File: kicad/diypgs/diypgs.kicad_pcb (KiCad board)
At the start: 2 copper layers, 150 x 66 mm, 15 parts, among them SW1 SW_Push_Dual, SW2 SW_Push_Dual, SW3 SW_Push_Dual, SW4 SW_Push_Dual, SW5 SW_Push_Dual, SW6 SW_Push_Dual, U1 Nokia_5110_LCD

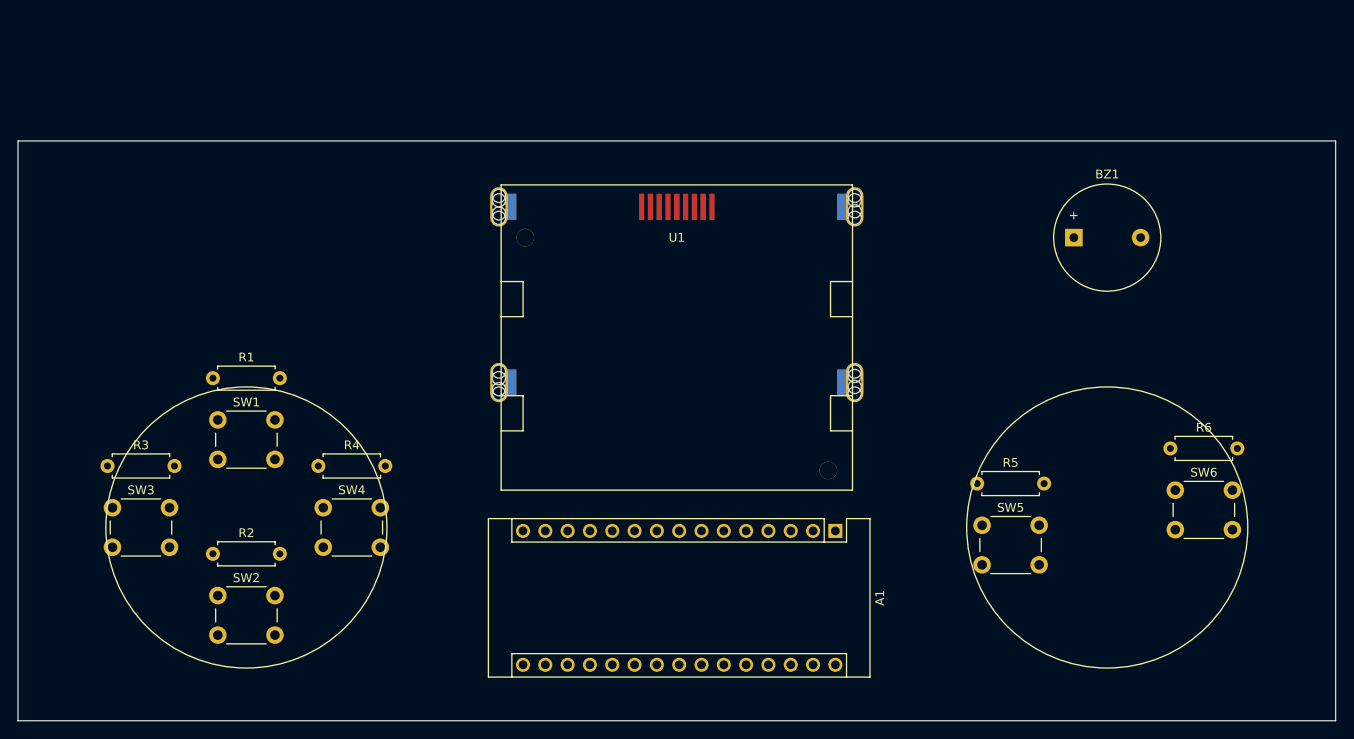
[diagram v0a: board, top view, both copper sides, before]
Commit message: Fix button pad number
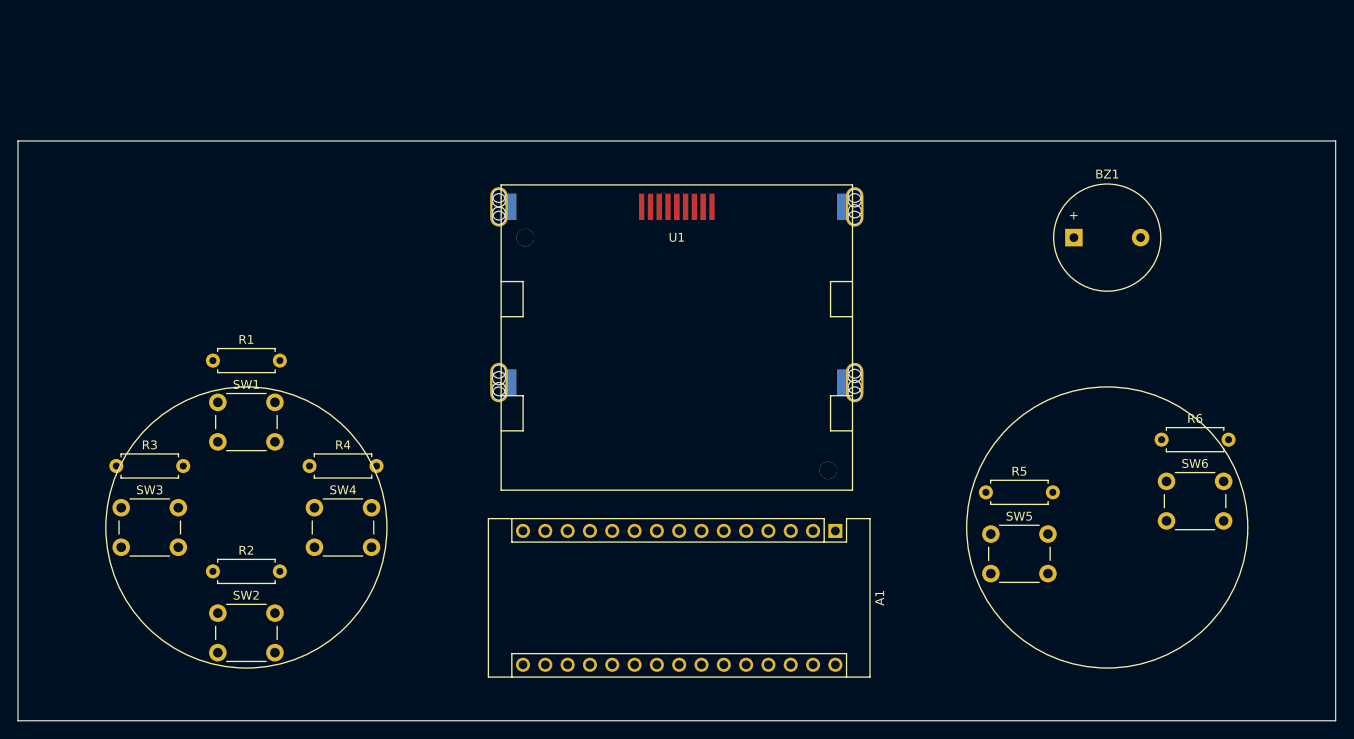
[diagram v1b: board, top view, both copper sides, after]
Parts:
- SW1, SW2, SW3, SW4, SW5, SW6: footprint Button_Switch_THT:SW_PUSH_6mm -> Footprints:SW_PUSH_6mm_ALT
- moved R1 2.00 mm to (72.2, 75.0)
- moved R2 2.00 mm to (72.2, 99.0)
- moved SW1 2.00 mm to (72.8, 79.8)
- moved SW2 2.00 mm to (72.8, 103.8)
- moved R5 1.41 mm to (160.2, 90.0)
- moved R6 1.41 mm to (180.2, 84.0)
- moved SW5 1.41 mm to (160.8, 94.8)
- moved SW6 1.41 mm to (180.8, 88.8)
- moved R3 1.00 mm to (61.2, 87.0)
- moved R4 1.00 mm to (83.2, 87.0)
- moved SW3 1.00 mm to (61.8, 91.8)
- moved SW4 1.00 mm to (83.8, 91.8)
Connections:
- R2 pad 1: Net-(R2-Pad1) -> Net-(SW2-Pad3)
- SW1 pad 1: Net-(R1-Pad1) -> +3V3
- SW1 pad 2: +3V3 -> unconnected-(SW1-Pad2)

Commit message: Add PCB tracks
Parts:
- moved SW5 7.91 mm to (167.2, 99.2), turned to 180 degrees
- moved SW6 7.91 mm to (187.2, 93.2), turned to 180 degrees
- moved R2 7.62 mm to (79.8, 99.0), turned to 180 degrees
- moved R5 7.62 mm to (167.8, 90.0), turned to 180 degrees
- moved R6 7.62 mm to (187.8, 84.0), turned to 180 degrees
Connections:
- A1 pad 10: /ARDUINO_PAD_B_PIN -> /ARDUINO_PAD_RIGHT_PIN
- A1 pad 11: /ARDUINO_BUZZER_PIN -> /ARDUINO_PAD_LEFT_PIN
- A1 pad 12: /ARDUINO_DC_PIN -> /ARDUINO_PAD_DOWN_PIN
- A1 pad 13: /ARDUINO_RESET_PIN -> /ARDUINO_PAD_UP_PIN
- A1 pad 5: /ARDUINO_PAD_UP_PIN -> /ARDUINO_PAD_B_PIN
- A1 pad 6: /ARDUINO_PAD_DOWN_PIN -> /ARDUINO_PAD_A_PIN
- A1 pad 7: /ARDUINO_PAD_LEFT_PIN -> /ARDUINO_BUZZER_PIN
- A1 pad 8: /ARDUINO_PAD_RIGHT_PIN -> /ARDUINO_RESET_PIN
- A1 pad 9: /ARDUINO_PAD_A_PIN -> /ARDUINO_DC_PIN
- SW5 pad 4: /ARDUINO_PAD_A_PIN -> /ARDUINO_PAD_B_PIN
- SW6 pad 4: /ARDUINO_PAD_B_PIN -> /ARDUINO_PAD_A_PIN
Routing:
- net +3V3: track 0.00 -> 133.5 mm
- net GND: track 0.00 -> 110.8 mm
- net /ARDUINO_BUZZER_PIN: track 0.00 -> 64.9 mm
- net /ARDUINO_PAD_A_PIN: track 0.00 -> 53.4 mm
- net /ARDUINO_PAD_B_PIN: track 0.00 -> 29.3 mm
- net Net-(R6-Pad1): track 0.00 -> 4.98 mm
- net Net-(R5-Pad1): track 0.00 -> 4.98 mm

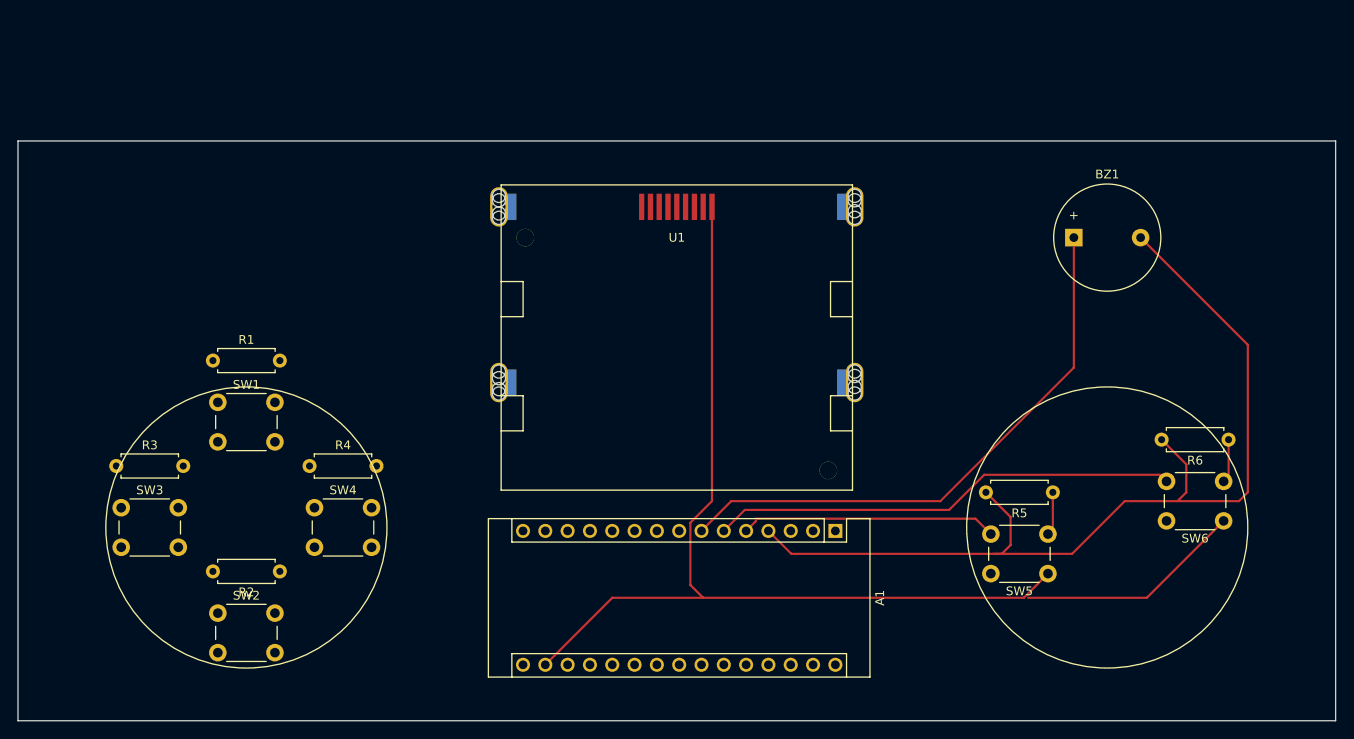
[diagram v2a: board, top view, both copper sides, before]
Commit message: Fix screen symbol and footprint
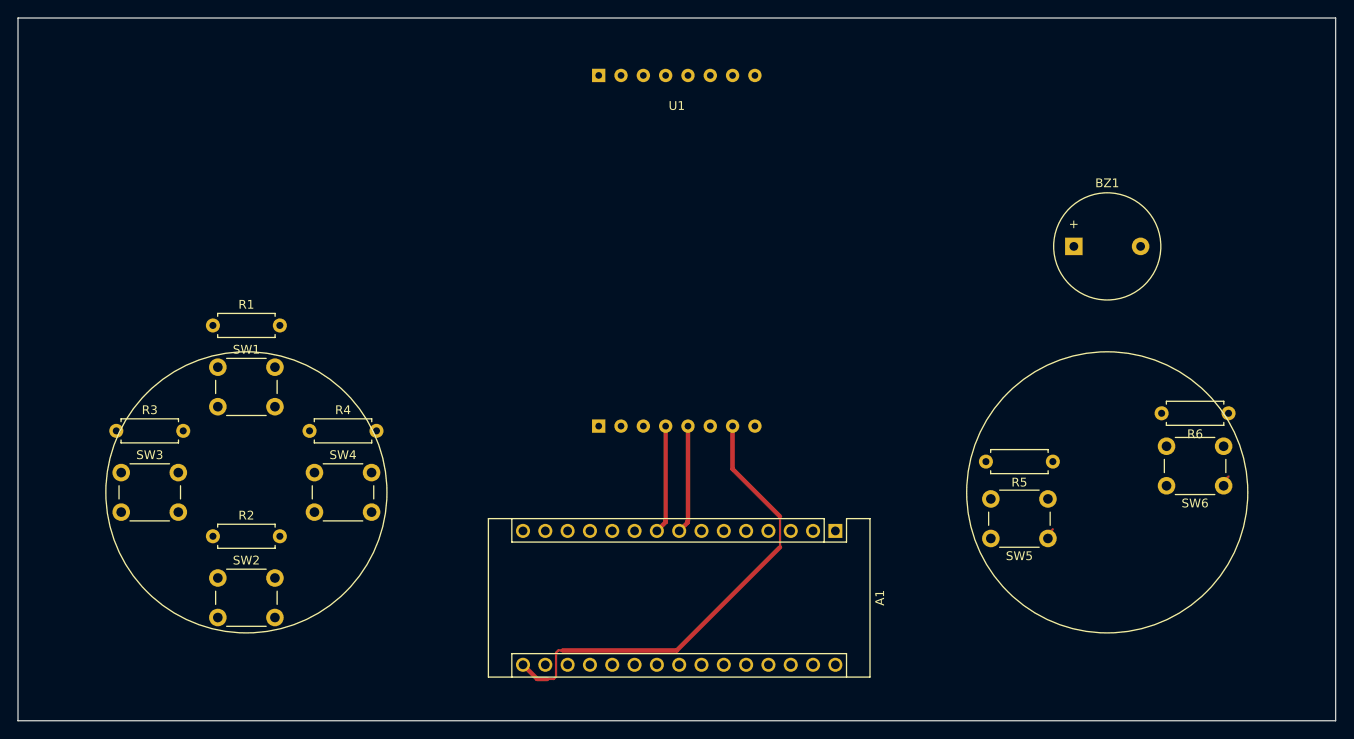
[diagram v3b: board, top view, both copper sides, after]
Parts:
- U1: value Nokia_5110_LCD -> Sparkfun - Graphic LCD 84x48 - Nokia 5110; footprint Nokia_5110-3310_LCD:Nokia_5110-3310_LCD -> Footprints:Sparkfun - Graphic LCD 84x48 - Nokia 5110
- moved U1 15.0 mm to (125.0, 40.0)
- moved R2 8.61 mm to (72.2, 95.0), turned to 0 degrees
- moved R1 4.00 mm to (72.2, 71.0)
- moved R3 4.00 mm to (61.2, 83.0)
- moved R4 4.00 mm to (83.2, 83.0)
- moved SW1 4.00 mm to (72.8, 75.8)
- moved SW2 4.00 mm to (72.8, 99.8)
- moved SW3 4.00 mm to (61.8, 87.8)
- moved SW4 4.00 mm to (83.8, 87.8)
- moved SW5 4.00 mm to (167.2, 95.2)
- moved SW6 4.00 mm to (187.2, 89.2)
- moved R5 3.50 mm to (167.8, 86.5)
- moved R6 3.00 mm to (187.8, 81.0)
- moved BZ1 1.00 mm to (170.2, 62.0)
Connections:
- A1 pad 8: /ARDUINO_RESET_PIN -> /ARDUINO_DC_PIN
- A1 pad 9: /ARDUINO_DC_PIN -> /ARDUINO_RESET_PIN
- U1 pad 1: /ARDUINO_RESET_PIN -> +3V3
- U1 pad 2: unconnected-(U1-Pad2) -> GND
- U1 pad 3: GND -> /ARDUINO_SS_PIN
- U1 pad 4: unconnected-(U1-Pad4) -> /ARDUINO_RESET_PIN
- U1 pad 5: /ARDUINO_SS_PIN -> /ARDUINO_DC_PIN
- U1 pad 6: /ARDUINO_DC_PIN -> /ARDUINO_MOSI_PIN
- U1 pad 7: /ARDUINO_MOSI_PIN -> /ARDUINO_SCK_PIN
- U1 pad 8: /ARDUINO_SCK_PIN -> unconnected-(U1-Pad8)
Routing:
- net +3V3: track 133.5 -> 1.58 mm
- net GND: track 110.8 -> 0.00 mm
- net /ARDUINO_BUZZER_PIN: track 64.9 -> 0.00 mm
- net /ARDUINO_SCK_PIN: track 0.00 -> 53.8 mm
- net /ARDUINO_PAD_A_PIN: track 53.4 -> 0.00 mm
- net /ARDUINO_PAD_B_PIN: track 29.3 -> 0.00 mm
- net /ARDUINO_DC_PIN: track 0.00 -> 12.7 mm
- net /ARDUINO_RESET_PIN: track 0.00 -> 12.4 mm
- net Net-(R6-Pad1): track 4.98 -> 0.00 mm
- net Net-(R5-Pad1): track 4.98 -> 0.00 mm
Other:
- board size 150 x 66 mm -> 150 x 80 mm

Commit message: All tracks routed
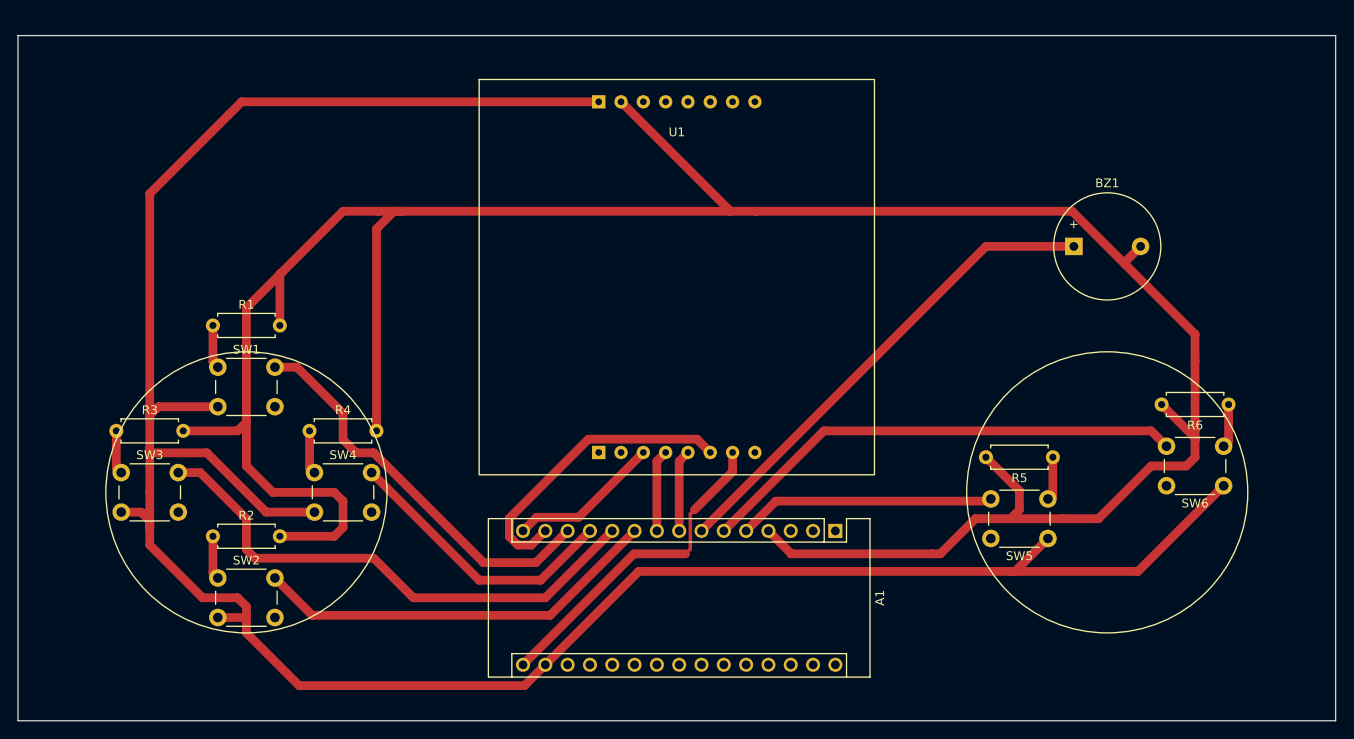
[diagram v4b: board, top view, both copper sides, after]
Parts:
- U1: value Sparkfun - Graphic LCD 84x48 - Nokia 5110 -> Nokia 5110 LCD
- moved U1 3.00 mm to (125.0, 43.0)
- moved R6 1.00 mm to (187.8, 80.0)
- moved R5 0.50 mm to (167.8, 86.0)
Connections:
- A1 pad 10: /ARDUINO_PAD_RIGHT_PIN -> /ARDUINO_PAD_DOWN_PIN
- A1 pad 12: /ARDUINO_PAD_DOWN_PIN -> /ARDUINO_PAD_RIGHT_PIN
- R3 pad 1: Net-(R3-Pad1) -> Net-(SW3-Pad1)
- R4 pad 1: Net-(R4-Pad1) -> Net-(SW4-Pad1)
- SW1 pad 1: +3V3 -> Net-(R1-Pad1)
- SW1 pad 2: unconnected-(SW1-Pad2) -> /ARDUINO_PAD_UP_PIN
- SW1 pad 3: Net-(R1-Pad1) -> +3V3
- SW1 pad 4: /ARDUINO_PAD_UP_PIN -> unconnected-(SW1-Pad4)
- SW2 pad 1: +3V3 -> Net-(R2-Pad1)
- SW2 pad 2: unconnected-(SW2-Pad2) -> /ARDUINO_PAD_DOWN_PIN
- SW2 pad 3: Net-(R2-Pad1) -> +3V3
- SW2 pad 4: /ARDUINO_PAD_DOWN_PIN -> unconnected-(SW2-Pad4)
- SW3 pad 1: +3V3 -> Net-(SW3-Pad1)
- SW3 pad 2: unconnected-(SW3-Pad2) -> /ARDUINO_PAD_LEFT_PIN
- SW3 pad 3: Net-(R3-Pad1) -> +3V3
- SW3 pad 4: /ARDUINO_PAD_LEFT_PIN -> unconnected-(SW3-Pad4)
- SW4 pad 1: +3V3 -> Net-(SW4-Pad1)
- SW4 pad 2: unconnected-(SW4-Pad2) -> /ARDUINO_PAD_RIGHT_PIN
- SW4 pad 3: Net-(R4-Pad1) -> +3V3
- SW4 pad 4: /ARDUINO_PAD_RIGHT_PIN -> unconnected-(SW4-Pad4)
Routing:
- net GND: track 0.00 -> 303.3 mm
- net +3V3: track 1.58 -> 278.5 mm
- net /ARDUINO_PAD_LEFT_PIN: track 0.00 -> 60.5 mm
- net /ARDUINO_PAD_A_PIN: track 0.00 -> 55.8 mm
- net /ARDUINO_BUZZER_PIN: track 0.00 -> 55.8 mm
- net /ARDUINO_PAD_DOWN_PIN: track 0.00 -> 46.7 mm
- net /ARDUINO_PAD_UP_PIN: track 0.00 -> 45.8 mm
- net /ARDUINO_MOSI_PIN: track 0.00 -> 34.5 mm
- net /ARDUINO_PAD_RIGHT_PIN: track 0.00 -> 32.3 mm
- net /ARDUINO_PAD_B_PIN: track 0.00 -> 29.4 mm
- net /ARDUINO_SS_PIN: track 0.00 -> 17.4 mm
- net /ARDUINO_SCK_PIN: track 53.8 -> 37.5 mm
- net Net-(SW4-Pad1): track 0.00 -> 4.98 mm
- net Net-(SW3-Pad1): track 0.00 -> 4.98 mm
- net Net-(R6-Pad1): track 0.00 -> 4.98 mm
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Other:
- board size 150 x 80 mm -> 150 x 78 mm
